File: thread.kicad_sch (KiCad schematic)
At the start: 25 parts, among them J3001 Conn_Coaxial, J3002 TC2050, J3003 Conn_01x06_Pin, U3001 nRF52840, Y3001 32.768kHz, Y3002 32MHz

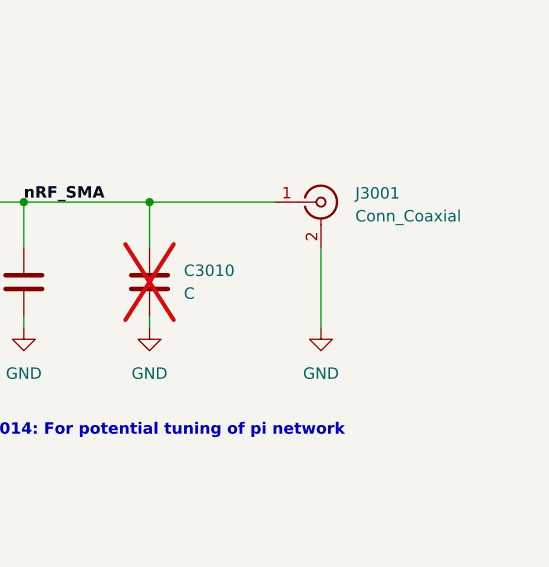
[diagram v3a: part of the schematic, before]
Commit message: Added many more footprints
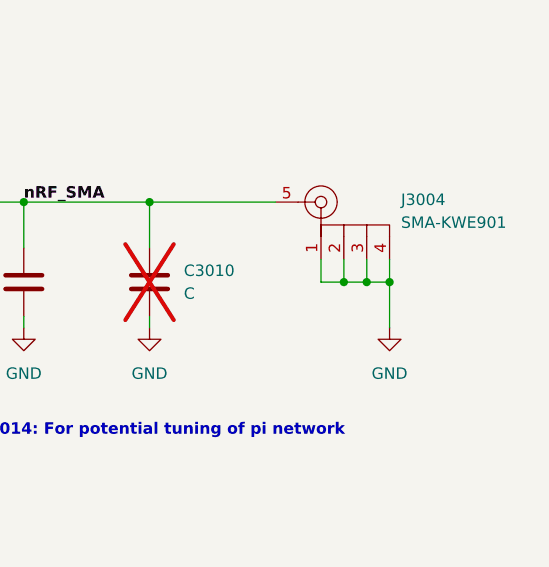
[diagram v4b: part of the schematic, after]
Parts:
- removed J3001: Conn_Coaxial, symbol Connector:Conn_Coaxial
- added J3004: SMA-KWE901, SoftServicesFootprintLibrary:SMA-KWE901, symbol SoftServicesSymbolLibrary:SMA-KWE901
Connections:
- net GND: now also J3004.1, J3004.2, J3004.3, J3004.4
- net nRF_SMA: now also J3004.5
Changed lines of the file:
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@@
+	)
+	(junction
+		(at 318.77 115.57)
+		(diameter 0)
+		(color 0 0 0 0)
 	)
 	(junction
@@
 	)
 	(junction
+		(at 321.31 115.57)
+		(diameter 0)
+		(color 0 0 0 0)
+	)
+	(junction
 		(at 275.59 59.69)
 		(diameter 0)
@@
 	)
 	(junction
+		(at 323.85 115.57)
+		(diameter 0)
+		(color 0 0 0 0)
+	)
+	(junction
 		(at 288.29 190.5)
 		(diameter 0)
@@
 	(wire
 		(pts
+			(xy 316.23 113.03) (xy 316.23 115.57)
+		)
+		(stroke
+			(width 0)
+			(type default)
+		)
+	)
+	(wire
+		(pts
 			(xy 250.19 228.6) (xy 229.87 228.6)
 		)
@@
 	(wire
 		(pts
+			(xy 316.23 115.57) (xy 318.77 115.57)
+		)
+		(stroke
+			(width 0)
+			(type default)
+		)
+	)
+	(wire
+		(pts
 			(xy 297.18 106.68) (xy 283.21 106.68)
 		)
@@
 	(wire
 		(pts
+			(xy 323.85 115.57) (xy 323.85 113.03)
+		)
+		(stroke
+			(width 0)
+			(type default)
+		)
+	)
+	(wire
+		(pts
 			(xy 292.1 185.42) (xy 288.29 185.42)
 		)
@@
 	(wire
 		(pts
+			(xy 318.77 115.57) (xy 321.31 115.57)
+		)
+		(stroke
+			(width 0)
+			(type default)
+		)
+	)
+	(wire
+		(pts
 			(xy 297.18 119.38) (xy 297.18 120.65)
 		)
@@
 	(wire
 		(pts
-			(xy 316.23 111.76) (xy 316.23 120.65)
-		)
-		(stroke
-			(width 0)
-			(type default)
-		)
-	)
-	(wire
-		(pts
 			(xy 138.43 95.25) (xy 138.43 52.07)
 		)
@@
 	(wire
 		(pts
+			(xy 321.31 115.57) (xy 323.85 115.57)
+		)
+		(stroke
+			(width 0)
+			(type default)
+		)
+	)
+	(wire
+		(pts
 			(xy 90.17 224.79) (xy 109.22 224.79)
 		)
@@
 	(wire
 		(pts
+			(xy 323.85 115.57) (xy 323.85 120.65)
+		)
+		(stroke
+			(width 0)
+			(type default)
+		)
+	)
+	(wire
+		(pts
 			(xy 78.74 69.85) (xy 66.04 69.85)
 		)
@@
 	(wire
 		(pts
+			(xy 318.77 113.03) (xy 318.77 115.57)
+		)
+		(stroke
+			(width 0)
+			(type default)
+		)
+	)
+	(wire
+		(pts
 			(xy 193.04 132.08) (xy 213.36 132.08)
 		)
@@
 		(pts
 			(xy 193.04 106.68) (xy 260.35 106.68)
+		)
+		(stroke
+			(width 0)
+			(type default)
+		)
+	)
+	(wire
+		(pts
+			(xy 321.31 113.03) (xy 321.31 115.57)
 		)
 		(stroke
@@
 	(symbol
 		(lib_id "power:GND")
-		(at 316.23 120.65 0)
+		(at 323.85 120.65 0)
 		(mirror y)
 		(unit 1)
@@
 		(fields_autoplaced yes)
 		(property "Reference" "#PWR03015"
-			(at 316.23 127 0)
+			(at 323.85 127 0)
 			(effects
 				(font
@@
 		)
 		(property "Value" "GND"
-			(at 316.23 125.73 0)
+			(at 323.85 125.73 0)
 			(effects
 				(font
@@
 		)
 		(property "Footprint" ""
-			(at 316.23 120.65 0)
+			(at 323.85 120.65 0)
 			(effects
 				(font
@@
 		)
 		(property "Datasheet" ""
-			(at 316.23 120.65 0)
+			(at 323.85 120.65 0)
 			(effects
 				(font
@@
 		)
 		(property "Description" "Power symbol creates a global label with name \"GND\" , ground"
-			(at 316.23 120.65 0)
+			(at 323.85 120.65 0)
 			(effects
 				(font
@@
 				(path "/b43b7bca-e50d-42ec-8ff0-e0016dfefe0a/ab846a80-6f2e-4d25-9090-1f6af1d6fbdd"
 					(reference "L3002")
+					(unit 1)
+				)
+			)
+		)
+	)
+	(symbol
+		(lib_id "SoftServicesSymbolLibrary:SMA-KWE901")
+		(at 316.23 106.68 0)
+		(unit 1)
+		(exclude_from_sim no)
+		(in_bom yes)
+		(on_board yes)
+		(dnp no)
+		(fields_autoplaced yes)
+		(property "Reference" "J3004"
+			(at 325.12 106.4168 0)
+			(effects
+				(font
+					(size 1.27 1.27)
+				)
+				(justify left)
+			)
+		)
+		(property "Value" "SMA-KWE901"
+			(at 325.12 108.9568 0)
+			(effects
+				(font
+					(size 1.27 1.27)
+				)
+				(justify left)
+			)
+		)
+		(property "Footprint" "SoftServicesFootprintLibrary:SMA-KWE901"
+			(at 316.23 106.68 0)
+			(effects
+				(font
+					(size 1.27 1.27)
+				)
+				(hide yes)
+			)
+		)
+		(property "Datasheet" ""
+			(at 316.23 106.68 0)
+			(effects
+				(font
+					(size 1.27 1.27)
+				)
+				(hide yes)
+			)
+		)
+		(property "Description" ""
+			(at 316.23 106.68 0)
+			(effects
+				(font
+					(size 1.27 1.27)
+				)
+				(hide yes)
+			)
+		)
+		(pin "4"
+		)
+		(pin "3"
+		)
+		(pin "2"
+		)
+		(pin "1"
+		)
+		(pin "5"
+		)
+		(instances
+			(project ""
+				(path "/b43b7bca-e50d-42ec-8ff0-e0016dfefe0a/ab846a80-6f2e-4d25-9090-1f6af1d6fbdd"
+					(reference "J3004")
 					(unit 1)
 				)
@@
 					(unit 1)
 				)
-			)
-		)
-	)
-	(symbol
-		(lib_id "Connector:Conn_Coaxial")
-		(at 316.23 106.68 0)
-		(unit 1)
-		(exclude_from_sim no)
-		(in_bom yes)
-		(on_board yes)
-		(dnp no)
-		(fields_autoplaced yes)
-		(property "Reference" "J3001"
-			(at 320.04 105.7031 0)
-			(effects
-				(font
-					(size 1.27 1.27)
-				)
-				(justify left)
-			)
-		)
-		(property "Value" "Conn_Coaxial"
-			(at 320.04 108.2431 0)
-			(effects
-				(font
-					(size 1.27 1.27)
-				)
-				(justify left)
-			)
-		)
-		(property "Footprint" ""
-			(at 316.23 106.68 0)
-			(effects
-				(font
-					(size 1.27 1.27)
-				)
-				(hide yes)
-			)
-		)
-		(property "Datasheet" "~"
-			(at 316.23 106.68 0)
-			(effects
-				(font
-					(size 1.27 1.27)
-				)
-				(hide yes)
-			)
-		)
-		(property "Description" "coaxial connector (BNC, SMA, SMB, SMC, Cinch/RCA, LEMO, ...)"
-			(at 316.23 106.68 0)
-			(effects
-				(font
-					(size 1.27 1.27)
-				)
-				(hide yes)
-			)
-		)
-		(pin "1"
-		)
-		(pin "2"
-		)
-		(instances
-			(project ""
-				(path "/b43b7bca-e50d-42ec-8ff0-e0016dfefe0a/ab846a80-6f2e-4d25-9090-1f6af1d6fbdd"
-					(reference "J3001")
-					(unit 1)
-				)

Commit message: More footprints
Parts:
- X3002: renamed from Y3002; footprint (none) -> Crystal:Crystal_SMD_2016-4Pin_2.0x1.6mm
- renumbered Y3001 to X3001
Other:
- note added: "ABS07-32.768KHZ-9-T (Maybe)"
- note added: "XRCGB32M000F1H01R0"
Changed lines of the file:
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@@
 	(generator_version "9.0")
 	(paper "A3")
+	(text "XRCGB32M000F1H01R0"
+		(exclude_from_sim no)
+		(at 41.148 152.908 0)
+		(effects
+			(font
+				(size 1.27 1.27)
+				(thickness 0.254)
+				(bold yes)
+			)
+		)
+	)
 	(text "C3014: For potential tuning of pi network"
 		(exclude_from_sim no)
@@
 		)
 	)
+	(text "ABS07-32.768KHZ-9-T (Maybe)"
+		(exclude_from_sim no)
+		(at 256.794 146.05 0)
+		(effects
+			(font
+				(size 1.27 1.27)
+				(thickness 0.254)
+				(bold yes)
+			)
+		)
+	)
 	(text "VSS_PA is radio GND"
 		(exclude_from_sim no)
@@
 		(dnp no)
 		(fields_autoplaced yes)
-		(property "Reference" "Y3002"
+		(property "Reference" "X3002"
 			(at 69.85 146.05 0)
 			(effects
@@
 			)
 		)
-		(property "Footprint" ""
+		(property "Footprint" "Crystal:Crystal_SMD_2016-4Pin_2.0x1.6mm"
 			(at 69.85 153.67 0)
 			(effects
@@
 			(project ""
 				(path "/b43b7bca-e50d-42ec-8ff0-e0016dfefe0a/ab846a80-6f2e-4d25-9090-1f6af1d6fbdd"
-					(reference "Y3002")
+					(reference "X3002")
 					(unit 1)
 				)
@@
 		(dnp no)
 		(fields_autoplaced yes)
-		(property "Reference" "Y3001"
+		(property "Reference" "X3001"
 			(at 234.95 116.84 0)
 			(effects
@@
 			(project ""
 				(path "/b43b7bca-e50d-42ec-8ff0-e0016dfefe0a/ab846a80-6f2e-4d25-9090-1f6af1d6fbdd"
-					(reference "Y3001")
+					(reference "X3001")
 					(unit 1)
 				)

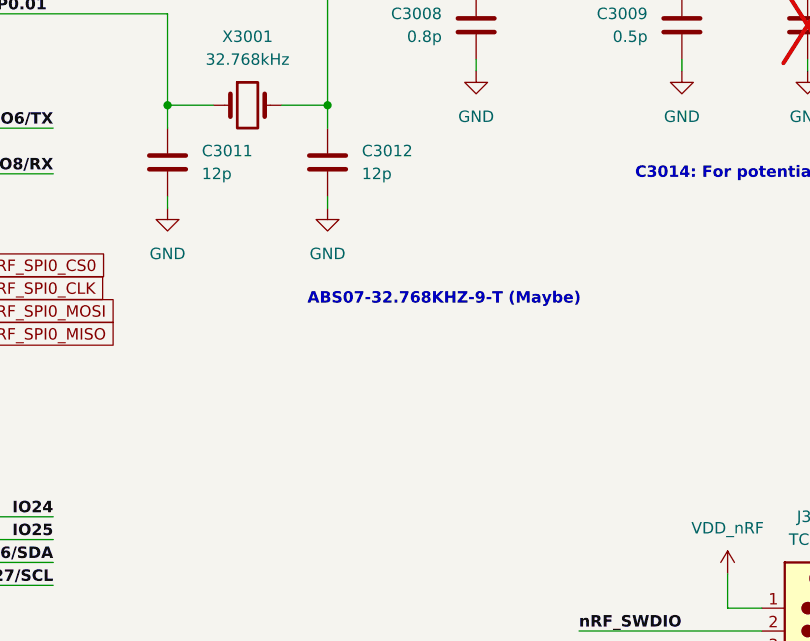
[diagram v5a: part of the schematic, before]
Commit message: Finished IC and crystal footprints
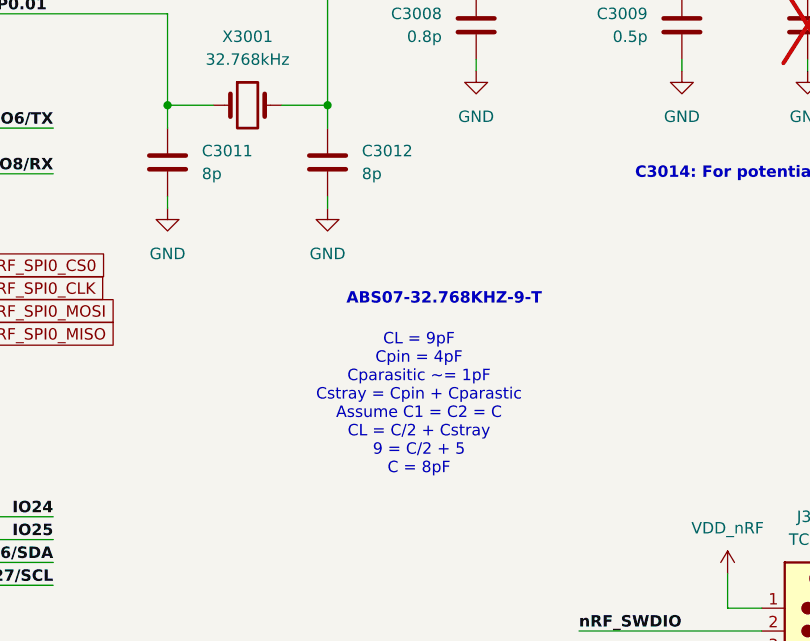
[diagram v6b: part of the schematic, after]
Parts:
- C3011, C3012: value 12p -> 8p
- J3003: footprint (none) -> Connector_PinHeader_2.54mm:PinHeader_1x06_P2.54mm_Vertical
- X3001: footprint (none) -> Crystal:Crystal_SMD_3215-2Pin_3.2x1.5mm
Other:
- note added: "ABS07-32.768KHZ-9-T"
- note added: "CL = 9pF Cpin = 4pF Cparasitic ~= 1pF Cstray = Cpin + Cparastic Assume C1 = C2 = C CL = C/2 + Cstray 9 = C/2 + 5 C = 8pF"
- note removed: "ABS07-32.768KHZ-9-T (Maybe)"
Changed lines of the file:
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@@
 	(generator_version "9.0")
 	(paper "A3")
+	(text "CL = 9pF\nCpin = 4pF\nCparasitic ~= 1pF\nCstray = Cpin + Cparastic\nAssume C1 = C2 = C\nCL = C/2 + Cstray\n9 = C/2 + 5\nC = 8pF"
+		(exclude_from_sim no)
+		(at 254 157.734 0)
+		(effects
+			(font
+				(size 1.27 1.27)
+			)
+		)
+	)
 	(text "XRCGB32M000F1H01R0"
 		(exclude_from_sim no)
@@
 		)
 	)
-	(text "ABS07-32.768KHZ-9-T (Maybe)"
+	(text "ABS07-32.768KHZ-9-T"
 		(exclude_from_sim no)
 		(at 256.794 146.05 0)
@@
 			)
 		)
-		(property "Value" "12p"
+		(property "Value" "8p"
 			(at 229.87 132.0799 0)
 			(effects
@@
 			)
 		)
-		(property "Value" "12p"
+		(property "Value" "8p"
 			(at 247.65 132.0799 0)
 			(effects
@@
 			)
 		)
-		(property "Footprint" ""
+		(property "Footprint" "Connector_PinHeader_2.54mm:PinHeader_1x06_P2.54mm_Vertical"
 			(at 255.27 223.52 0)
 			(effects
@@
 			)
 		)
-		(property "Footprint" ""
+		(property "Footprint" "Crystal:Crystal_SMD_3215-2Pin_3.2x1.5mm"
 			(at 234.95 124.46 0)
 			(effects

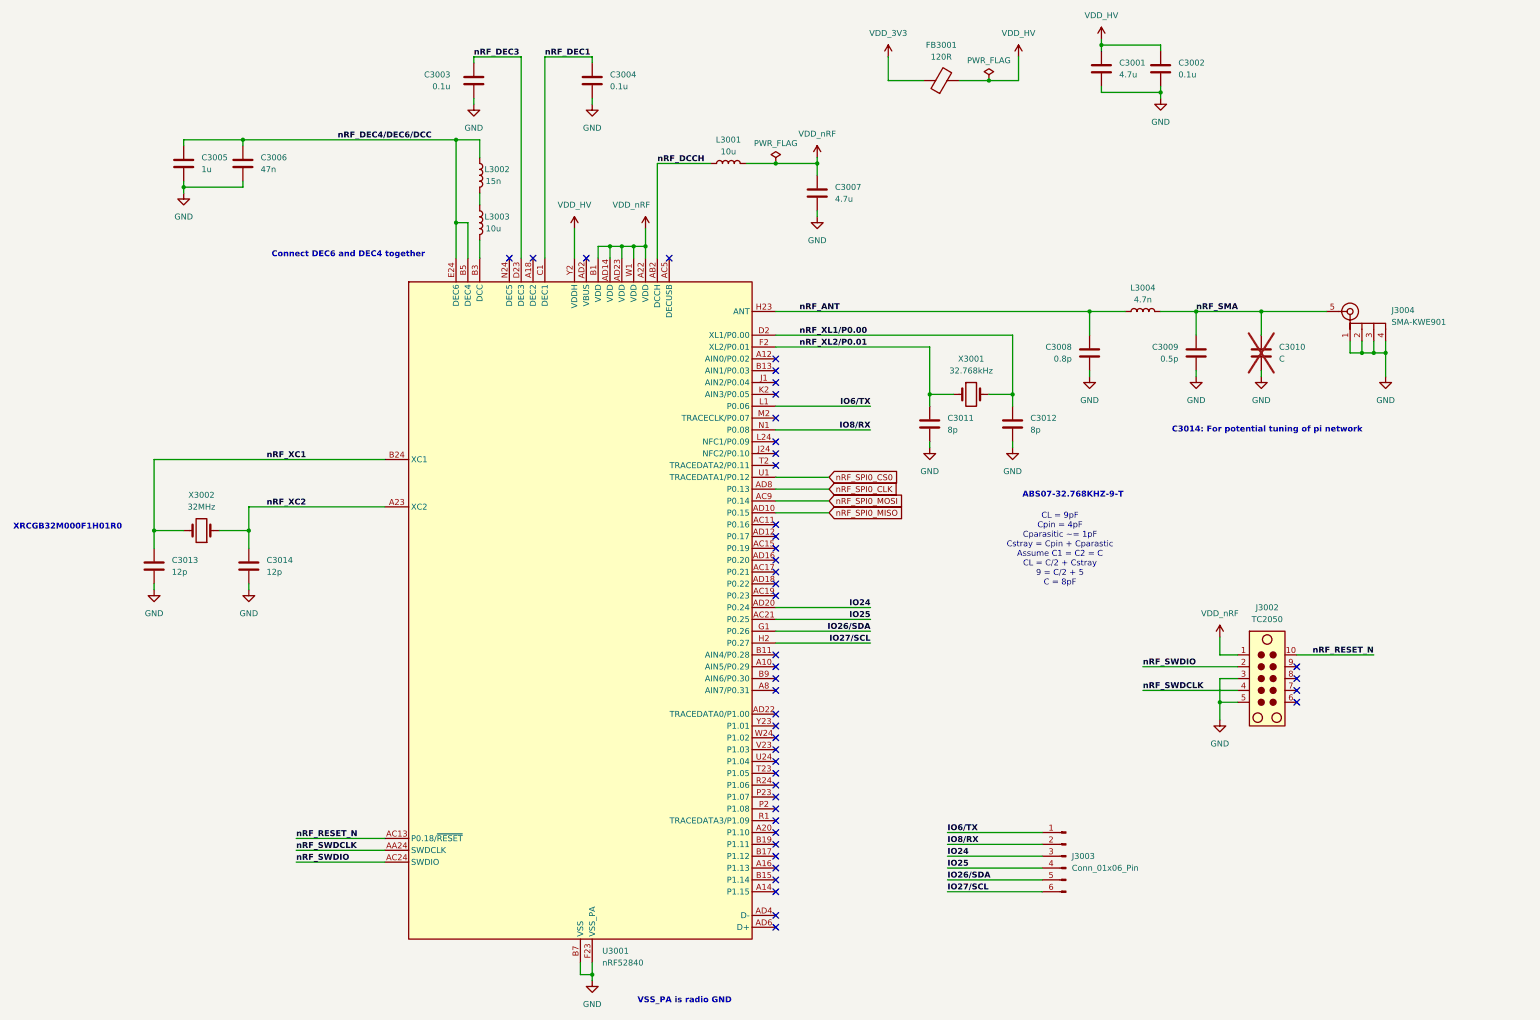
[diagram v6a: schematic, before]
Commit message: Added almost all passive component footprints
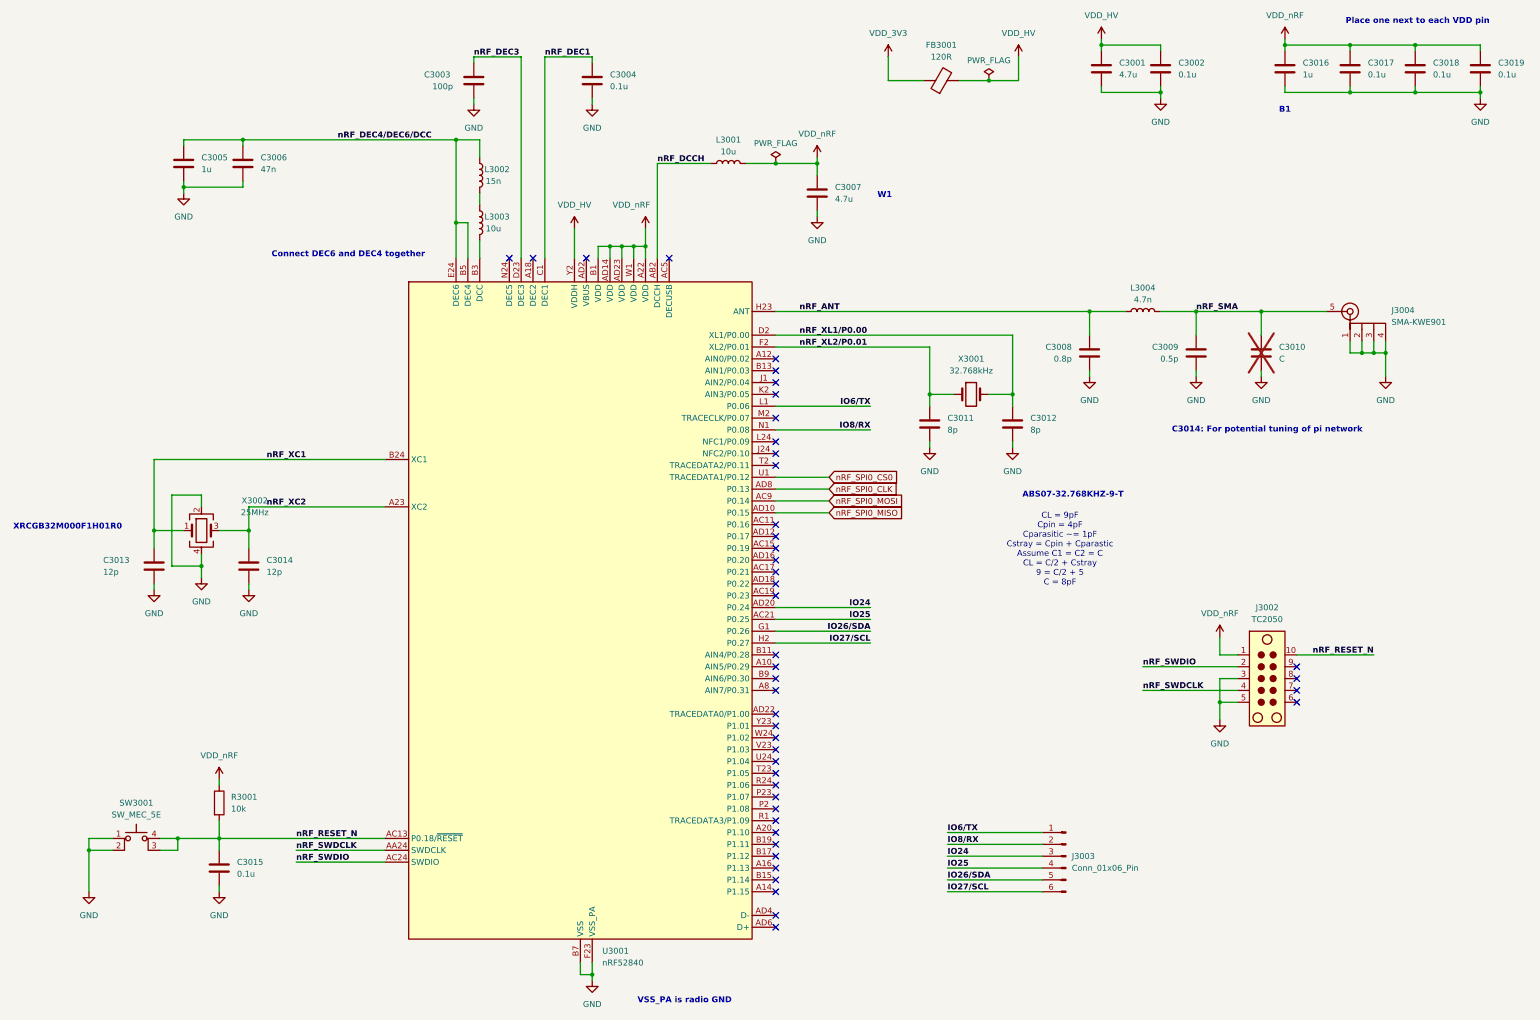
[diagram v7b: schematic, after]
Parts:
- removed X3002: 32MHz, Crystal:Crystal_SMD_2016-4Pin_2.0x1.6mm, symbol Device:Crystal
- added C3015, C3017, C3018, C3019: 0.1u, Capacitor_SMD:C_0201_0603Metric, symbol Device:C
- added C3016: 1u, Capacitor_SMD:C_0603_1608Metric, symbol Device:C
- added R3001: 10k, Resistor_SMD:R_0201_0603Metric, symbol Device:R
- added SW3001: SW_MEC_5E, symbol Switch:SW_MEC_5E
- added X3002: 25MHz, Crystal:Crystal_SMD_2016-4Pin_2.0x1.6mm, symbol Device:Crystal_GND24
- C3001: footprint (none) -> Capacitor_SMD:C_0402_1005Metric
- C3002, C3004, C3006, C3008, C3009, C3011, C3012, C3013, C3014: footprint (none) -> Capacitor_SMD:C_0201_0603Metric
- C3003: value 0.1u -> 100p; footprint (none) -> Capacitor_SMD:C_0201_0603Metric
- C3005, C3007: footprint (none) -> Capacitor_SMD:C_0603_1608Metric
- FB3001: footprint (none) -> Resistor_SMD:R_0402_1005Metric
- L3001, L3003: footprint (none) -> Inductor_SMD:L_0603_1608Metric
- L3002: footprint (none) -> Inductor_SMD:L_0402_1005Metric
- L3004: footprint (none) -> Inductor_SMD:L_0201_0603Metric
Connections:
- net GND: now also C3015.2, C3016.2, C3017.2, C3018.2, C3019.2, SW3001.1, SW3001.2, X3002.2, X3002.4
- net VDD_nRF: now also C3016.1, C3017.1, C3018.1, C3019.1, R3001.1
- net nRF_RESET_N: now also C3015.1, R3001.2, SW3001.3 (K), SW3001.4 (A)
- net nRF_XC1: now also X3002.1
- net nRF_XC2: now also X3002.3
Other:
- note added: "B1"
- note added: "Place one next to each VDD pin"
- note added: "W1"
